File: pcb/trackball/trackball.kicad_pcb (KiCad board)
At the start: 2 copper layers, 22 parts, among them U1 AN48841B, U2 AN48841B, U3 AN48841B, U4 AN48841B

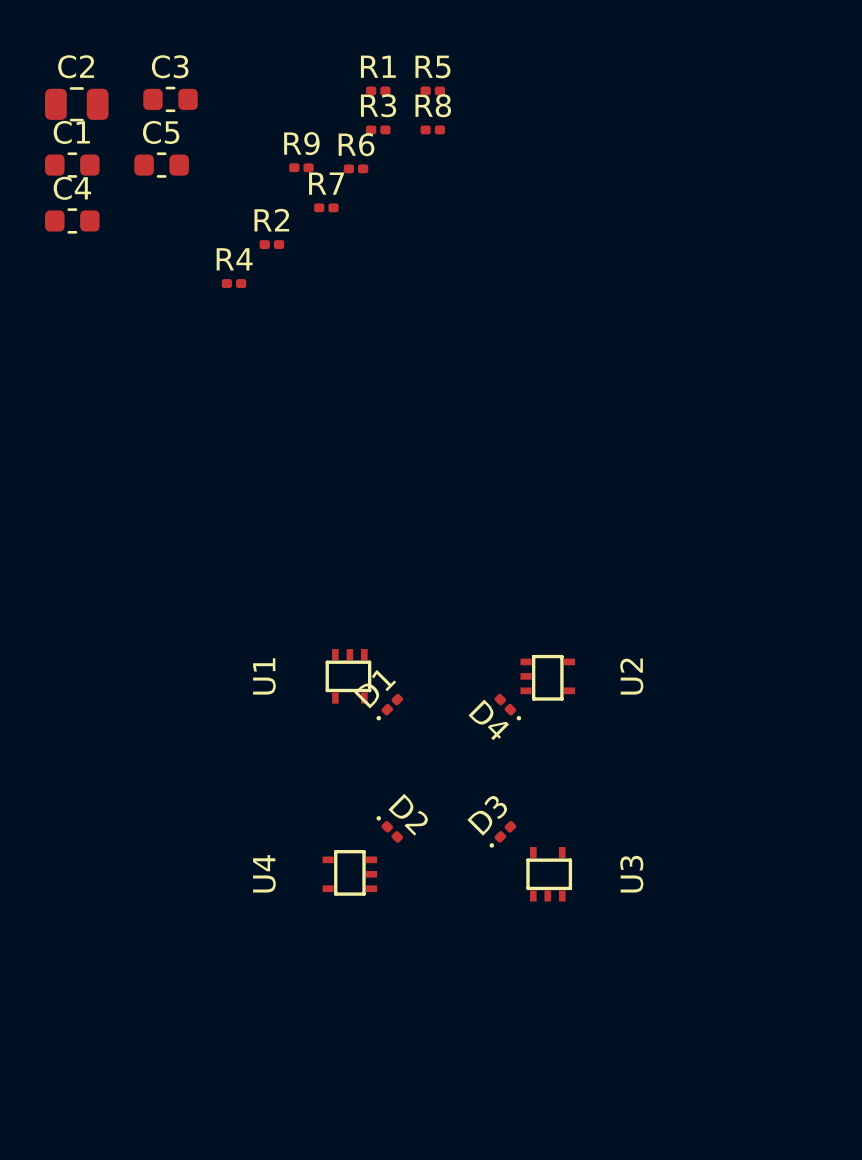
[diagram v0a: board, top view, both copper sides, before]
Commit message: complete trackball breakout
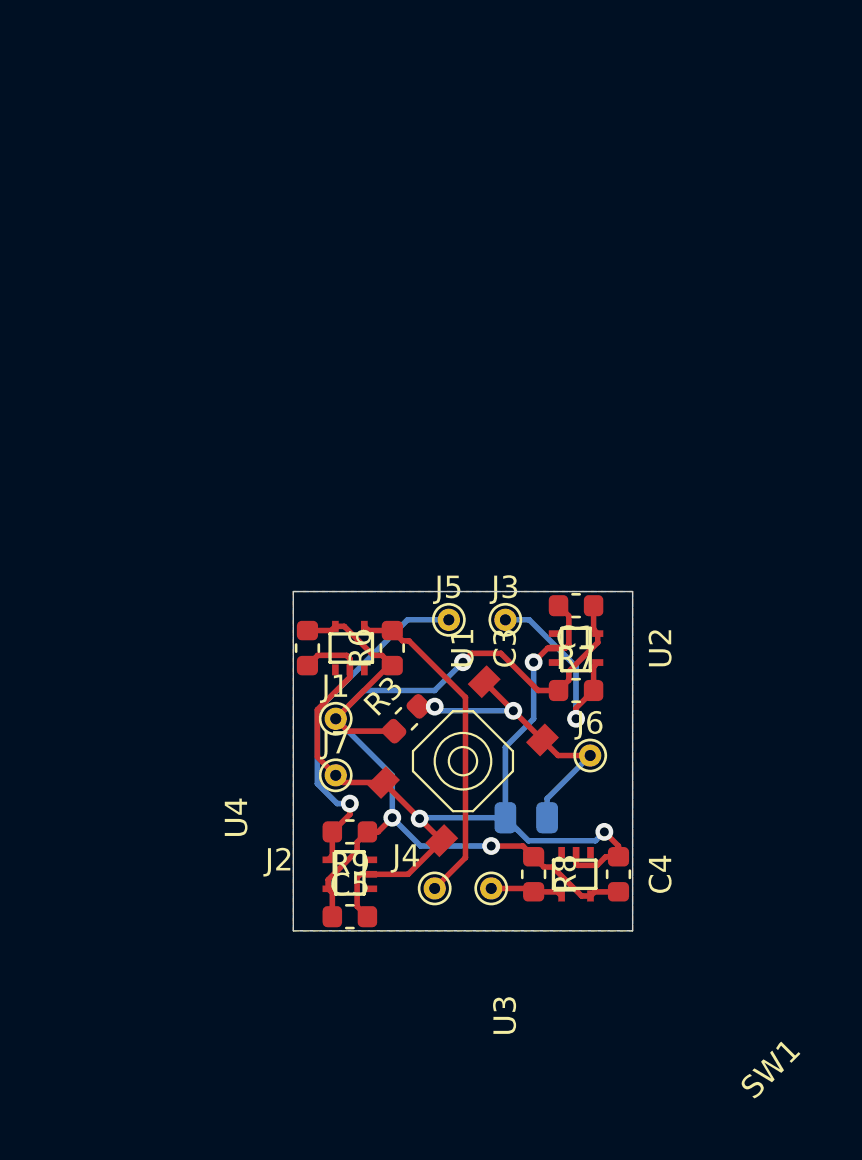
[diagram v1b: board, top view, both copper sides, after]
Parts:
- removed D1, D2, D3, D4: LED, LED_SMD:LED_0201_0603Metric
- removed R1, R2, R4, R5: R, Resistor_SMD:R_0201_0603Metric
- added J1: Conn_01x01_Female, TestPoint:TestPoint_THTPad_D1.0mm_Drill0.5mm, F.Cu at (136.5, 83.2)
- added J2: Conn_01x01_Female, TestPoint:TestPoint_THTPad_D1.0mm_Drill0.5mm, F.Cu at (141.0, 90.8)
- added J3: Conn_01x01_Female, TestPoint:TestPoint_THTPad_D1.0mm_Drill0.5mm, F.Cu at (144.1, 78.7)
- added J4: Conn_01x01_Female, TestPoint:TestPoint_THTPad_D1.0mm_Drill0.5mm, F.Cu at (143.5, 90.8)
- added J5: Conn_01x01_Female, TestPoint:TestPoint_THTPad_D1.0mm_Drill0.5mm, F.Cu at (141.6, 78.7)
- added J6: Conn_01x01_Female, TestPoint:TestPoint_THTPad_D1.0mm_Drill0.5mm, F.Cu at (148.0, 84.8)
- added J7: Conn_01x01_Female, TestPoint:TestPoint_THTPad_D1.0mm_Drill0.5mm, F.Cu at (136.5, 85.7)
- added SW1: BTN, folivora:Film_Switch_4X4X0.8MM, F.Cu at (142.2, 85.1)
- C2: moved to B.Cu
- R3, R6, R7, R8, R9: footprint Resistor_SMD:R_0201_0603Metric -> Resistor_SMD:R_0603_1608Metric
- moved C4 38.2 mm to (149.2, 90.2), turned to 90 degrees
- moved C2 37.9 mm to (145.1, 87.6), turned to 180 degrees
- moved C5 34.8 mm to (137.2, 92.1)
- moved R8 33.7 mm to (145.4, 90.2), turned to 270 degrees
- moved C1 30.1 mm to (147.3, 78.1), turned to 180 degrees
- moved R9 29.9 mm to (137.2, 88.3), turned to 180 degrees
- moved R3 26.5 mm to (139.7, 83.2), turned to 45 degrees
- moved C3 25.4 mm to (135.3, 80.0), turned to 270 degrees
- moved R7 24.4 mm to (147.3, 81.9)
- moved R6 21.6 mm to (139.1, 80.0), turned to 90 degrees
- moved U2 1.80 mm to (147.3, 80.0)
- moved U1 1.27 mm to (137.2, 80.0), turned to 0 degrees
- moved U3 1.27 mm to (147.3, 90.2), turned to 180 degrees
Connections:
- net Net-(R6-Pad2) renamed /UP
- net Net-(R7-Pad2) renamed /RIGHT
- net Net-(R8-Pad2) renamed /DOWN
- net Net-(R9-Pad2) renamed /LEFT
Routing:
- net +5V: track 0.00 -> 50.7 mm, vias 0 -> 3
- net GND: track 0.00 -> 45.0 mm, vias 0 -> 3
- net /LEFT: track 0.00 -> 15.7 mm, vias 0 -> 1
- net /UP: track 0.00 -> 15.0 mm
- net /BTN: track 0.00 -> 14.1 mm, vias 0 -> 2
- net /RIGHT: track 0.00 -> 9.32 mm, vias 0 -> 1
- net /DOWN: track 0.00 -> 3.30 mm
- added copper zone on B.Cu, net GND
- added copper zone on F.Cu, net GND
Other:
- board outline added: 15.2 x 15.2 mm

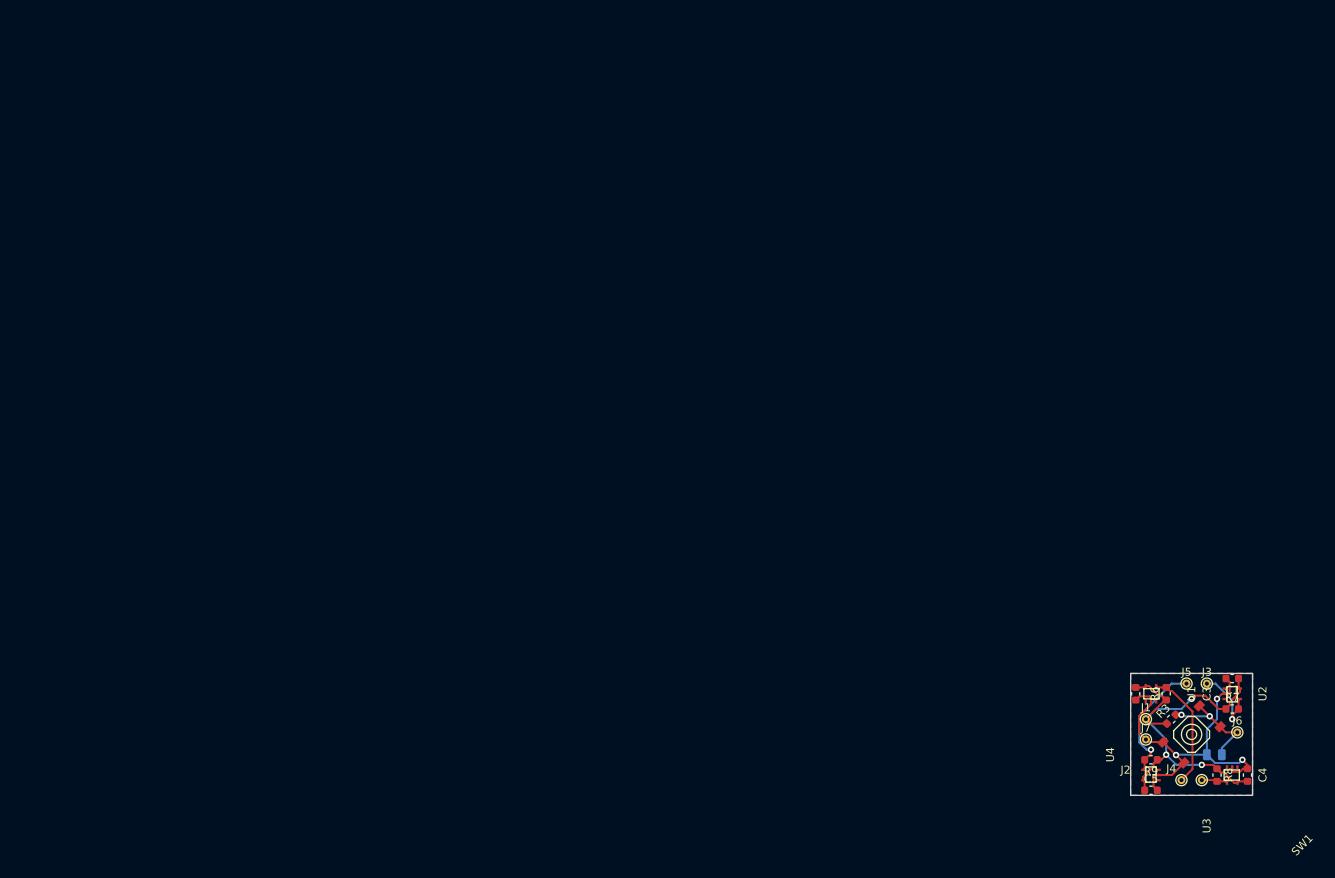
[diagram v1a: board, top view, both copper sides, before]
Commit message: trackball breakout
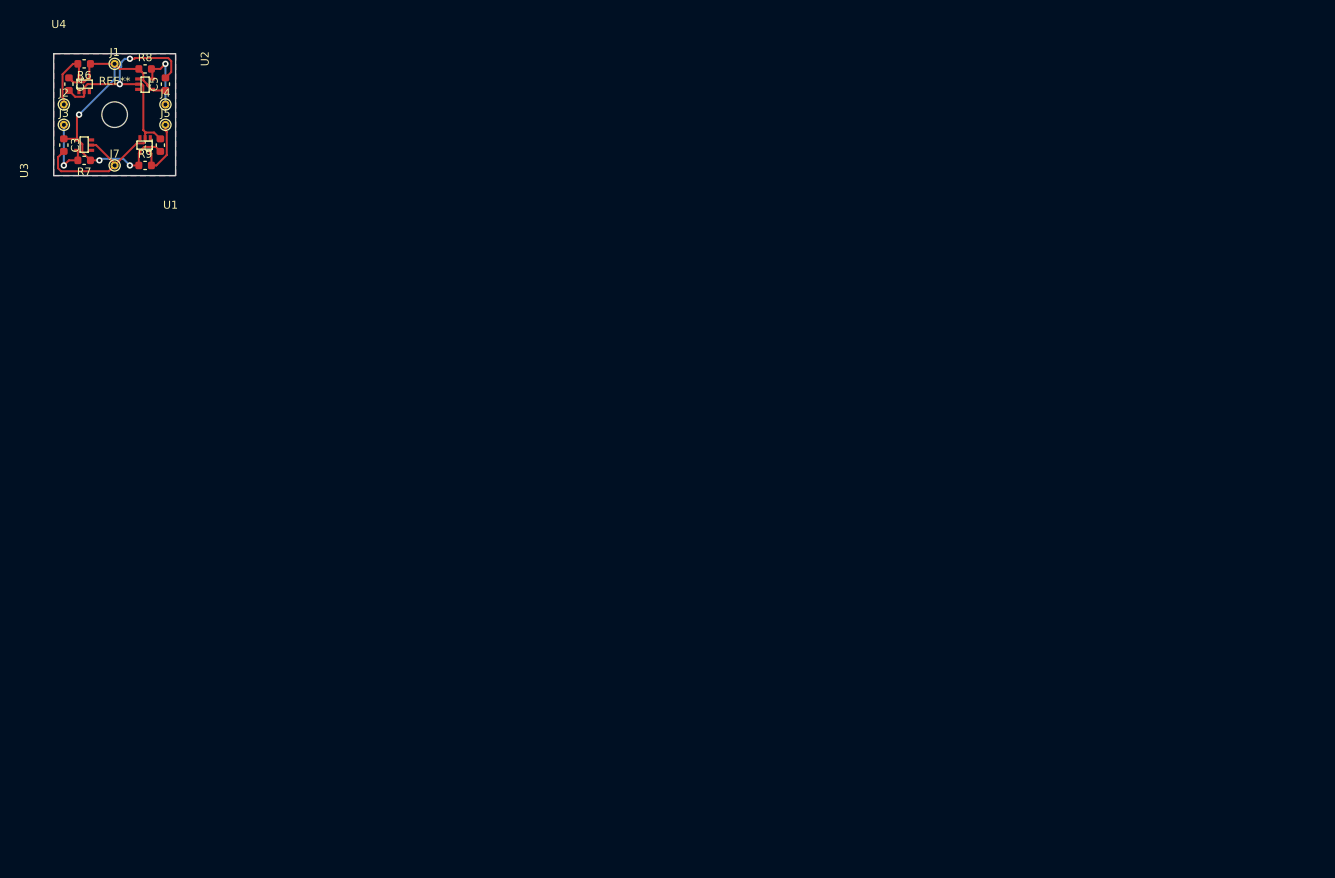
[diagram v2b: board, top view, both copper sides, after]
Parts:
- removed C2: 1uF, Capacitor_SMD:C_0805_2012Metric
- removed J6: Conn_01x01_Female, TestPoint:TestPoint_THTPad_D1.0mm_Drill0.5mm
- removed R3: 10k, Resistor_SMD:R_0603_1608Metric
- removed SW1: BTN, folivora:Film_Switch_4X4X0.8MM
- added REF**: MountingHole_3.2mm_M3, MountingHole:MountingHole_3.2mm_M3, F.Cu at (7.62, 7.62)
- J1: value Conn_01x01_Female -> 5V
- J2: value Conn_01x01_Female -> UP
- J3: value Conn_01x01_Female -> R
- J4: value Conn_01x01_Female -> D
- J5: value Conn_01x01_Female -> L
- J7: value Conn_01x01_Female -> GND
- U1, U2, U3, U4: footprint folivora:SMINI-5DE -> folivora:SMINI_5DE
- moved C4 170.8 mm to (1.91, 3.81), turned to 270 degrees
- moved J2 163.2 mm to (1.27, 6.35)
- moved U3 161.0 mm to (11.4, 3.81), turned to 270 degrees
- moved R8 160.4 mm to (11.4, 1.91), turned to 0 degrees
- moved R7 159.1 mm to (3.81, 13.3), turned to 180 degrees
- moved U2 159.1 mm to (3.81, 11.4), turned to 90 degrees
- moved J3 159.0 mm to (1.27, 8.89)
- moved R6 156.5 mm to (3.81, 1.27), turned to 180 degrees
- moved J4 154.6 mm to (14.0, 6.35)
- moved U1 153.6 mm to (3.81, 3.81)
- moved J1 152.7 mm to (7.62, 1.27)
- moved C5 151.5 mm to (14.0, 3.81), turned to 90 degrees
- moved C3 150.5 mm to (1.27, 11.4)
- moved C1 149.7 mm to (13.3, 11.4), turned to 90 degrees
- moved U4 148.4 mm to (11.4, 11.4), turned to 180 degrees
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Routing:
- net /BTN: track 14.1 -> 0.00 mm, vias 2 -> 0
- net /LEFT: track 15.7 -> 8.00 mm, vias 1 -> 0
- net /UP: track 15.0 -> 8.00 mm
- net +5V: track 50.7 -> 43.9 mm
- net GND: track 45.0 -> 51.2 mm, vias 3 -> 2
- net /DOWN: track 3.30 -> 8.40 mm, vias 0 -> 1
- net /RIGHT: track 9.32 -> 8.40 mm
- added copper zone on F.Cu, net (none)
- removed copper zone on F.Cu, net GND

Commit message: production pcb
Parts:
- added REF**: Micro_hole, folivora:Micro_hole, F.Cu at (3.81, 7.62)
- added REF**: Micro_hole, folivora:Micro_hole, F.Cu at (11.4, 7.62)
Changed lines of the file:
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@@
     (thickness 1.6)
     (drawings 4)
-    (tracks 112)
+    (tracks 113)
     (zones 0)
-    (modules 19)
+    (modules 21)
     (nets 15)
   )
@@
       (outputformat 1)
       (mirror false)
-      (drillshape 1)
+      (drillshape 0)
       (scaleselection 1)
-      (outputdirectory ""))
+      (outputdirectory "gerber/"))
   )
   (net 0 "")
@@
     (add_net "Net-(U4-Pad3)")
   )
+  (module folivora:Micro_hole (layer F.Cu)
+    (at 3.81 7.62)
+    (fp_text reference REF** (at 0 2.54) (layer F.SilkS)
+      (effects (font (size 1 1) (thickness 0.15)))
+    )
+    (fp_text value Micro_hole (at 0 3.81) (layer F.Fab)
+      (effects (font (size 1 1) (thickness 0.15)))
+    )
+    (pad 1 thru_hole circle (at 0 0) (size 0.5 0.5) (drill 0.5) (layers *.Cu *.Mask))
+  )
+  (module folivora:Micro_hole (layer F.Cu)
+    (at 11.43 7.62)
+    (fp_text reference REF** (at 0 2.54) (layer F.SilkS)
+      (effects (font (size 1 1) (thickness 0.15)))
+    )
+    (fp_text value Micro_hole (at 0 3.81) (layer F.Fab)
+      (effects (font (size 1 1) (thickness 0.15)))
+    )
+    (pad 1 thru_hole circle (at 0 0) (size 0.5 0.5) (drill 0.5) (layers *.Cu *.Mask))
+  )
   (module MountingHole:MountingHole_3.2mm_M3 (layer F.Cu)
     (at 7.62 7.62)
@@
   (segment (start 10.105 1.905) (end 10.6425 1.905) (width 0.25) (layer F.Cu) (net 1))
   (segment (start 7.62 1.27) (end 8.255 1.905) (width 0.25) (layer F.Cu) (net 1))
-  (via (at 3.175 7.62) (size 0.8) (drill 0.4) (layers F.Cu B.Cu) (net 1))
-  (segment (start 2.91 10.78) (end 2.91 7.885) (width 0.25) (layer F.Cu) (net 1))
-  (segment (start 2.91 7.885) (end 3.175 7.62) (width 0.25) (layer F.Cu) (net 1))
-  (segment (start 7.62 3.175) (end 7.62 1.27) (width 0.25) (layer B.Cu) (net 1))
-  (segment (start 3.175 7.62) (end 7.62 3.175) (width 0.25) (layer B.Cu) (net 1))
   (segment (start 12.33 4.46) (end 12.18 4.46) (width 0.25) (layer F.Cu) (net 1))
   (segment (start 11.104112 2.366612) (end 10.6425 1.905) (width 0.25) (layer F.Cu) (net 1))
@@
   (segment (start 11.205001 3.335001) (end 11.205001 2.467501) (width 0.25) (layer F.Cu) (net 1))
   (segment (start 11.73 3.86) (end 11.205001 3.335001) (width 0.25) (layer F.Cu) (net 1))
+  (via (at 2.54 7.62) (size 0.8) (drill 0.4) (layers F.Cu B.Cu) (net 1))
+  (segment (start 2.91 10.78) (end 2.91 7.99) (width 0.25) (layer F.Cu) (net 1))
+  (segment (start 2.91 7.99) (end 2.54 7.62) (width 0.25) (layer F.Cu) (net 1))
+  (segment (start 7.62 2.54) (end 2.54 7.62) (width 0.25) (layer B.Cu) (net 1))
+  (segment (start 7.62 1.27) (end 7.62 2.54) (width 0.25) (layer B.Cu) (net 1))
   (segment (start 11.43 9.93) (end 11.43 10.53) (width 0.25) (layer F.Cu) (net 2))
   (segment (start 11.505001 9.854999) (end 11.43 9.93) (width 0.25) (layer F.Cu) (net 2))
@@
   (segment (start 1.27 12.2175) (end 0.544998 12.942502) (width 0.25) (layer F.Cu) (net 2))
   (segment (start 0.921998 14.695002) (end 6.894998 14.695002) (width 0.25) (layer F.Cu) (net 2))
-  (segment (start 11.205001 9.554999) (end 11.205001 3.999999) (width 0.25) (layer F.Cu) (net 2))
-  (segment (start 11.505001 9.854999) (end 11.205001 9.554999) (width 0.25) (layer F.Cu) (net 2))
-  (segment (start 11.015002 3.81) (end 10.53 3.81) (width 0.25) (layer F.Cu) (net 2))
-  (segment (start 11.205001 3.999999) (end 11.015002 3.81) (width 0.25) (layer F.Cu) (net 2))
+  (segment (start 12.547499 7.886497) (end 12.547499 9.854999) (width 0.25) (layer F.Cu) (net 2))
+  (segment (start 11.015002 3.81) (end 11.205001 3.999999) (width 0.25) (layer F.Cu) (net 2))
+  (segment (start 11.205001 6.543999) (end 12.547499 7.886497) (width 0.25) (layer F.Cu) (net 2))
+  (segment (start 11.205001 3.999999) (end 11.205001 6.543999) (width 0.25) (layer F.Cu) (net 2))
+  (segment (start 10.53 3.81) (end 11.015002 3.81) (width 0.25) (layer F.Cu) (net 2))
   (segment (start 3.16 1.4075) (end 3.0225 1.27) (width 0.25) (layer F.Cu) (net 11))
   (segment (start 3.16 2.91) (end 3.16 1.4075) (width 0.25) (layer F.Cu) (net 11))
